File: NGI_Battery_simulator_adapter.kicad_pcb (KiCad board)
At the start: 2 copper layers, 100 x 100 mm, 39 parts, among them J1 Screw_Terminal_01x20, J2 1725042, J3 Conn_01x05, J4 Screw_Terminal_01x20, J6 1725042

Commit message: gerber update
fix some DRC error, minor change
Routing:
- net /Cell_1-: track 88.3 -> 108.0 mm
- net /Cell_2+: track 67.8 -> 77.7 mm
- net /Cell_10+: track 149.7 -> 146.2 mm
- added copper zone on B.Cu, net /Cell_1-
- added copper zone on F.Cu, net /Cell_1-
- added copper zone on B.Cu, net /Cell_12+
- added copper zone on F.Cu, net /Cell_12+
- added copper zone on F.Cu, net /Cell_6+
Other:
- board text added: "Sofia - 2024.01"
- board text removed: "Sofia - 2023"
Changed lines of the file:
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@@
     )
   )
-  (gr_rect (start 50 70) (end 55 75)
-    (stroke (width 0.2) (type default)) (fill none) (layer "F.Cu"))
-  (gr_rect (start 50 90) (end 55 95)
-    (stroke (width 0.2) (type default)) (fill none) (layer "F.Cu"))
-  (gr_rect (start 55 45) (end 60 50)
-    (stroke (width 0.2) (type default)) (fill none) (layer "F.Cu"))
-  (gr_rect (start 55 90) (end 60 95)
-    (stroke (width 0.2) (type default)) (fill none) (layer "F.Cu"))
-  (gr_rect (start 50 45) (end 55 50)
-    (stroke (width 0.2) (type default)) (fill none) (layer "F.Cu"))
-  (gr_rect (start 50 65) (end 55 70)
-    (stroke (width 0.2) (type default)) (fill none) (layer "F.Cu"))
-  (gr_rect (start 55 65) (end 60 70)
-    (stroke (width 0.2) (type default)) (fill none) (layer "F.Cu"))
-  (gr_rect (start 55 70) (end 60 75)
-    (stroke (width 0.2) (type default)) (fill none) (layer "F.Cu"))
   (gr_circle (center 145 25) (end 141 25)
     (stroke (width 1) (type default)) (fill none) (layer "B.SilkS"))
@@
     (effects (font (size 1 1) (thickness 0.15)) (justify left bottom))
   )
-  (gr_text "Sofia - 2023" (at 81.25 27.4) (layer "F.SilkS" knockout)
+  (gr_text "Sofia - 2024.01" (at 81.25 27.4) (layer "F.SilkS" knockout)
     (effects (font (size 1.8 1.8) (thickness 0.45) bold) (justify left bottom))
   )
@@
     (style (thickness 0.1) (arrow_length 1.27) (text_position_mode 0) (extension_height 0.58642) (extension_offset 0.5) keep_text_aligned)
   )
+  (segment (start 145.33 36.75) (end 145.355 36.775) (width 2) (layer "F.Cu") (net 1))
+  (segment (start 135.5 40.25) (end 145.33 40.25) (width 2) (layer "F.Cu") (net 1))
   (segment (start 108.6 42.5) (end 108.6 47.5) (width 2) (layer "F.Cu") (net 1))
+  (segment (start 145.33 40.25) (end 145.355 40.275) (width 2) (layer "F.Cu") (net 1))
+  (segment (start 135.5 36.75) (end 145.33 36.75) (width 2) (layer "F.Cu") (net 1))
   (segment (start 145.28 36.85) (end 145.355 36.775) (width 1) (layer "B.Cu") (net 1))
   (segment (start 110 42.5) (end 112.225 40.275) (width 2) (layer "B.Cu") (net 1))
@@
   (segment (start 101.75 47.5) (end 105.1 47.5) (width 2) (layer "B.Cu") (net 2))
   (segment (start 101.6 47.5) (end 101.75 47.5) (width 2) (layer "B.Cu") (net 2))
+  (segment (start 135.5 47.25) (end 145.33 47.25) (width 2) (layer "F.Cu") (net 3))
+  (segment (start 145.33 47.25) (end 145.355 47.275) (width 2) (layer "F.Cu") (net 3))
   (segment (start 94.6 47.5) (end 98.1 47.5) (width 2) (layer "F.Cu") (net 3))
   (segment (start 94.6 42.5) (end 98.1 42.5) (width 2) (layer "F.Cu") (net 3))
-  (segment (start 145.355 47.275) (end 116.475 47.275) (width 2) (layer "B.Cu") (net 3))
   (segment (start 98.1 42.5) (end 98.1 47.5) (width 2) (layer "B.Cu") (net 3))
-  (segment (start 113 50.75) (end 99.971142 50.75) (width 2) (layer "B.Cu") (net 3))
+  (segment (start 94.6 42.5) (end 94.6 47.5) (width 2) (layer "B.Cu") (net 3))
+  (segment (start 118.85 50.75) (end 99.971142 50.75) (width 2) (layer "B.Cu") (net 3))
+  (segment (start 99.971142 50.75) (end 98.1 48.878858) (width 2) (layer "B.Cu") (net 3))
   (segment (start 98.1 48.878858) (end 98.1 47.5) (width 2) (layer "B.Cu") (net 3))
-  (segment (start 94.6 42.5) (end 94.6 47.5) (width 2) (layer "B.Cu") (net 3))
-  (segment (start 99.971142 50.75) (end 98.1 48.878858) (width 2) (layer "B.Cu") (net 3))
-  (segment (start 116.475 47.275) (end 113 50.75) (width 2) (layer "B.Cu") (net 3))
+  (segment (start 145.355 47.275) (end 122.325 47.275) (width 2) (layer "B.Cu") (net 3))
+  (segment (start 122.325 47.275) (end 118.85 50.75) (width 2) (layer "B.Cu") (net 3))
   (segment (start 91.1 49.85) (end 91.1 47.5) (width 2) (layer "F.Cu") (net 4))
   (segment (start 87.6 47.5) (end 91.1 47.5) (width 2) (layer "F.Cu") (net 4))
@@
   (segment (start 98 92.5) (end 98 97.5) (width 2) (layer "F.Cu") (net 11))
   (segment (start 94.5 97.5) (end 98 97.5) (width 2) (layer "F.Cu") (net 11))
+  (segment (start 94.4 88.6) (end 94.4 92.4) (width 2) (layer "F.Cu") (net 11))
   (segment (start 94.5 92.5) (end 98 92.5) (width 2) (layer "F.Cu") (net 11))
-  (segment (start 145.355 75.275) (end 106.325 75.275) (width 2) (layer "F.Cu") (net 11))
+  (segment (start 107.725 75.275) (end 94.4 88.6) (width 2) (layer "F.Cu") (net 11))
+  (segment (start 145.355 75.275) (end 107.725 75.275) (width 2) (layer "F.Cu") (net 11))
   (segment (start 94.4 92.4) (end 94.5 92.5) (width 2) (layer "F.Cu") (net 11))
-  (segment (start 106.325 75.275) (end 94.4 87.2) (width 2) (layer "F.Cu") (net 11))
-  (segment (start 94.4 87.2) (end 94.4 92.4) (width 2) (layer "F.Cu") (net 11))
   (segment (start 94.5 92.5) (end 97.5 92.5) (width 2) (layer "B.Cu") (net 11))
   (segment (start 94.5 92.5) (end 94.5 97.5) (width 2) (layer "B.Cu") (net 11))
   (segment (start 98 92) (end 98 97.5) (width 2) (layer "B.Cu") (net 11))
   (segment (start 97.5 92.5) (end 98 92) (width 2) (layer "B.Cu") (net 11))
-  (segment (start 98 89.45) (end 98 92.55) (width 1) (layer "B.Cu") (net 11))
+  (segment (start 98 83.75) (end 98 92.5) (width 2) (layer "B.Cu") (net 11))
   (segment (start 106.475 75.275) (end 98 83.75) (width 2) (layer "B.Cu") (net 11))
-  (segment (start 98 83.75) (end 98 92) (width 2) (layer "B.Cu") (net 11))
   (segment (start 145.355 75.275) (end 106.475 75.275) (width 2) (layer "B.Cu") (net 11))
   (segment (start 111.225 78.775) (end 101.5 88.5) (width 2) (layer "F.Cu") (net 12))
@@
     )
   )
+  (zone (net 13) (net_name "/Cell_12+") (layer "F.Cu") (hatch none 0.5)
+    (connect_pads yes (clearance 0.5))
+    (min_thickness 0.25) (filled_areas_thickness no)
+    (fill yes (thermal_gap 0.5) (thermal_bridge_width 0.5))
+    (polygon
+      (pts
+        (xy 107.453921 91.3)
+        (xy 113.2 91.3)
+        (xy 113.2 98.563752)
+        (xy 107.453921 98.563752)
+      )
+    )
+  )
+  (zone (net 7) (net_name "/Cell_6+") (layer "F.Cu") (hatch none 0.5)
+    (connect_pads yes (clearance 0.5))
+    (min_thickness 0.25) (filled_areas_thickness no)
+    (fill yes (thermal_gap 0.5) (thermal_bridge_width 0.5))
+    (polygon
+      (pts
+        (xy 65.853921 91.436248)
+        (xy 71.6 91.436248)
+        (xy 71.6 98.7)
+        (xy 65.853921 98.7)
+      )
+    )
+  )
+  (zone (net 1) (net_name "/Cell_1-") (layer "F.Cu") (hatch none 0.5)
+    (connect_pads yes (clearance 0.5))
+    (min_thickness 0.25) (filled_areas_thickness no)
+    (fill yes (thermal_gap 0.5) (thermal_bridge_width 0.5))
+    (polygon
+      (pts
+        (xy 107.353921 41.336248)
+        (xy 113.1 41.336248)
+        (xy 113.1 48.6)
+        (xy 107.353921 48.6)
+      )
+    )
+  )
   (zone (net 10) (net_name "/Cell_9+") (layer "F.Cu") (hatch none 0.5)
     (connect_pads yes (clearance 0.5))
@@
     )
   )
+  (zone (net 7) (net_name "/Cell_6+") (layer "F.Cu") (hatch none 0.5)
+    (connect_pads yes (clearance 0.5))
+    (min_thickness 0.25) (filled_areas_thickness no)
+    (fill yes (thermal_gap 0.5) (thermal_bridge_width 0.5))
+    (polygon
+      (pts
+        (xy 65.753921 41.336248)
+        (xy 71.5 41.336248)
+        (xy 71.5 48.6)
+        (xy 65.753921 48.6)
+      )
+    )
+  )
   (zone (net 9) (net_name "/Cell_8+") (layer "B.Cu") (hatch none 0.5)
     (connect_pads yes (clearance 0.5))
@@
     )
   )
+  (zone (net 1) (net_name "/Cell_1-") (layer "B.Cu") (hatch none 0.5)
+    (connect_pads yes (clearance 0.5))
+    (min_thickness 0.25) (filled_areas_thickness no)
+    (fill yes (thermal_gap 0.5) (thermal_bridge_width 0.5))
+    (polygon
+      (pts
+        (xy 107.2 41.3)
+        (xy 112.7 41.3)
+        (xy 112.7 48.6)
+        (xy 107.1 48.6)
+      )
+    )
+  )
   (zone (net 2) (net_name "/Cell_1+") (layer "B.Cu") (hatch none 0.5)
     (connect_pads yes (clearance 0.5))
@@
       )
     )
+  )
+  (zone (net 13) (net_name "/Cell_12+") (layer "B.Cu") (hatch none 0.5)
+    (connect_pads yes (clearance 0.5))
+    (min_thickness 0.25) (filled_areas_thickness no)
+    (fill yes (thermal_gap 0.5) (thermal_bridge_width 0.5))
+    (polygon
+      (pts
+        (xy 107.3 91.3)
+        (xy 112.8 91.3)
+        (xy 112.8 98.6)
+        (xy 107.2 98.6)
+      )
+    )

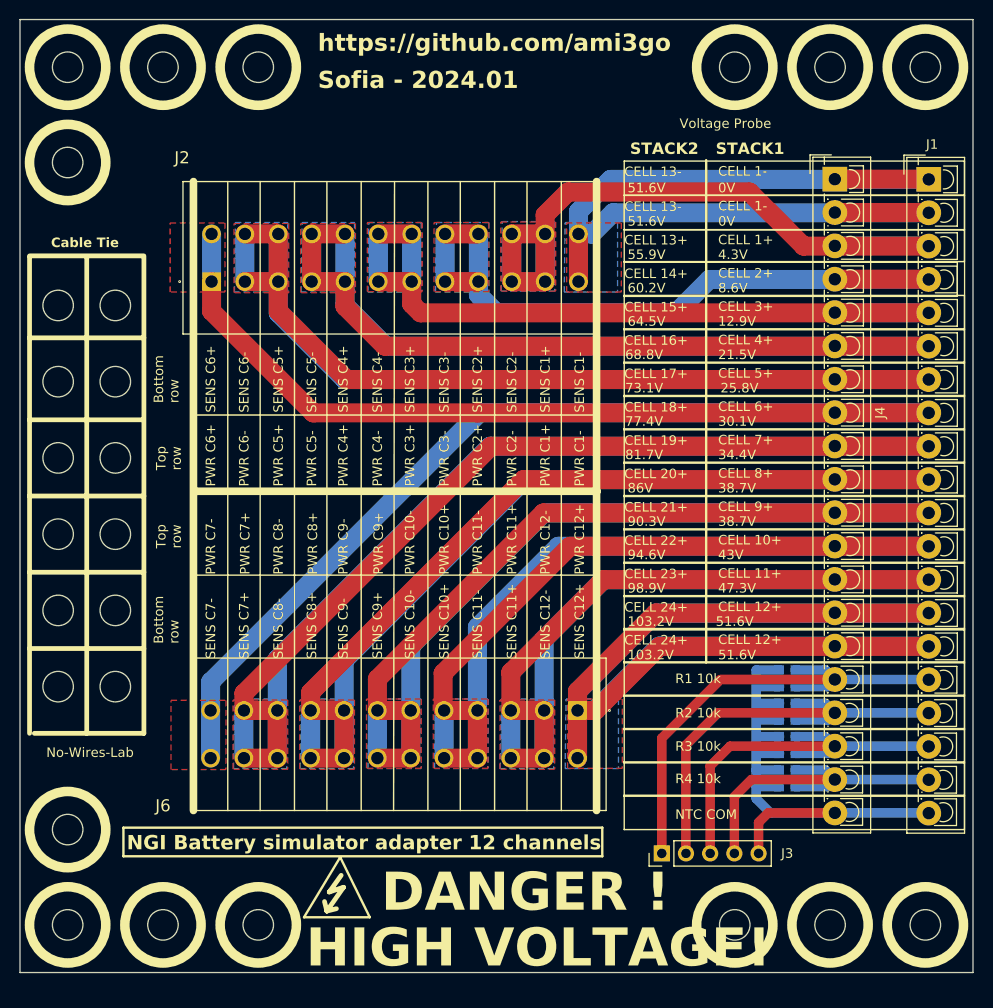
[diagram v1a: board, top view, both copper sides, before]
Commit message: update for Kicad 9
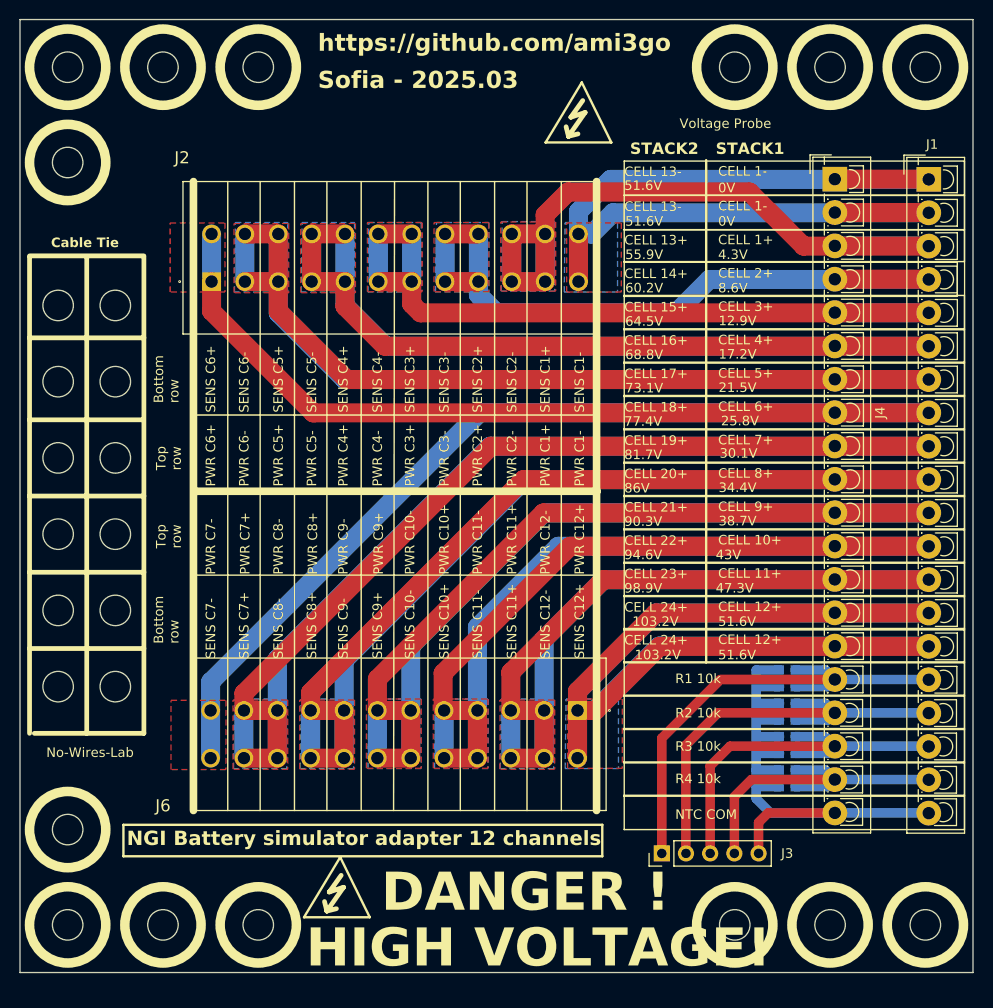
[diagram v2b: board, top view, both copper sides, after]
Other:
- board text added: "17.2V"
- board text added: "Sofia - 2025.03"
- board text removed: "Sofia - 2024.01"
